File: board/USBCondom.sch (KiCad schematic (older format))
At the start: 8 parts, among them P1 To_Source, P2 To_Phone

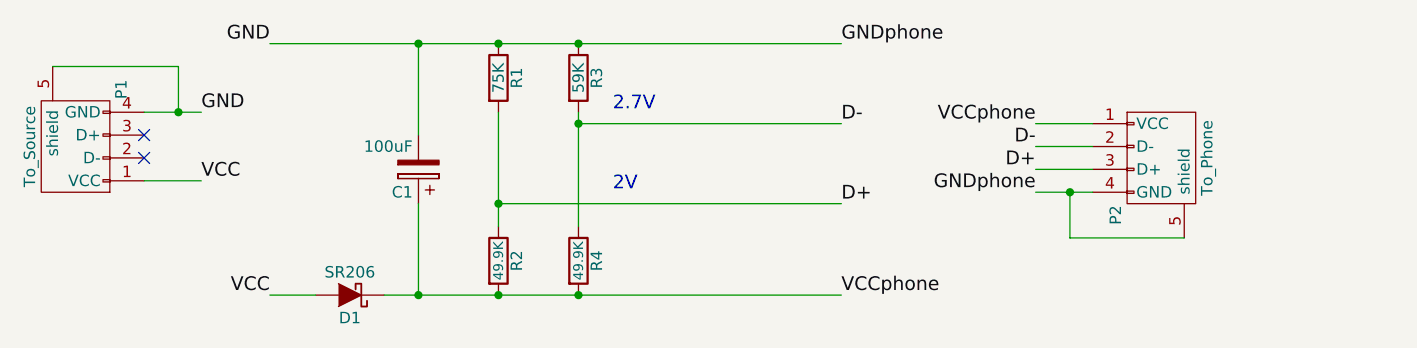
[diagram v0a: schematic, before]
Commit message: Update board to rev 2
Bugfixes:
* USB shields are no longer connected to GND

Updates:
* Changed C1 footprint to 1206_HandSoldering for larger pads
* Shrank down board size and made layout more compact
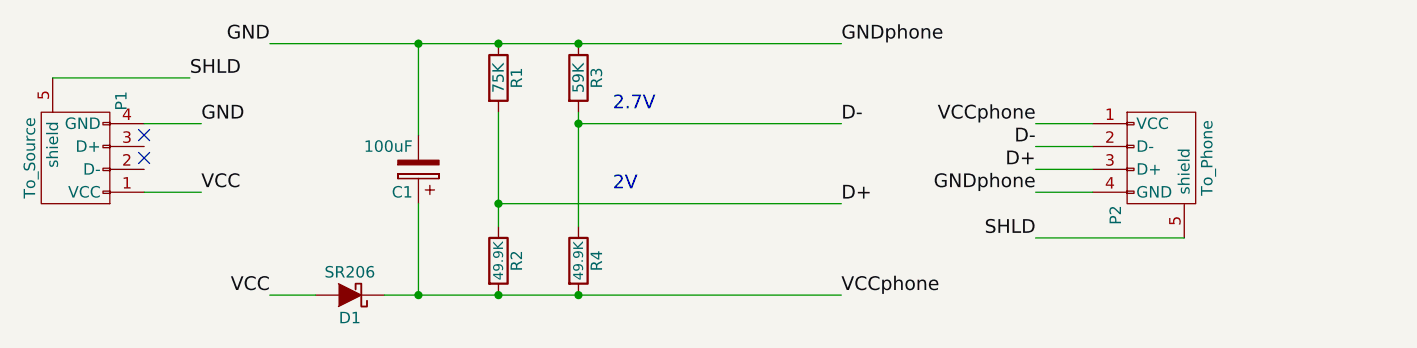
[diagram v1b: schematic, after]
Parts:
- C1: footprint Capacitors_SMD:C_1206 -> Capacitors_SMD:C_1206_HandSoldering
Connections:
- net GND: no longer P1.5 (shield), P2.5 (shield)
- new net SHLD: P1.5 (shield), P2.5 (shield)
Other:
- moved on the sheet: P1
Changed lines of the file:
@@
 Title "USB Condom"
 Date ""
-Rev "0.1"
+Rev "2"
 Comp "csammisrun"
 Comment1 ""
@@
 L USB_A P1
 U 1 1 58C0BE71
-P 1350 2800
-F 0 "P1" H 1550 2600 50  0000 C CNN
-F 1 "To_Source" H 1300 3000 50  0000 C CNN
-F 2 "Connect:USB_A" V 1300 2700 50  0001 C CNN
-F 3 "" V 1300 2700 50  0000 C CNN
-	1    1350 2800
+P 1350 2850
+F 0 "P1" H 1550 2650 50  0000 C CNN
+F 1 "To_Source" H 1300 3050 50  0000 C CNN
+F 2 "Connect:USB_A" V 1300 2750 50  0001 C CNN
+F 3 "" V 1300 2750 50  0000 C CNN
+	1    1350 2850
 	0    -1   -1   0
 $EndComp
@@
 F 0 "C1" H 2875 3050 50  0000 L CNN
 F 1 "100uF" H 2875 2850 50  0000 L CNN
-F 2 "Capacitors_SMD:C_1206" H 2888 2800 50  0001 C CNN
+F 2 "Capacitors_SMD:C_1206_HandSoldering" H 2888 2800 50  0001 C CNN
 F 3 "" H 2850 2950 50  0000 C CNN
 	1    2850 2950
@@
 	5800 2950 5550 2950
 Wire Wire Line
-	5550 3050 5800 3050
-Wire Wire Line
 	2850 3100 2850 3500
 Wire Wire Line
@@
 Connection ~ 2850 2400
 Connection ~ 2850 3500
-Wire Wire Line
-	5700 3050 5700 3250
-Wire Wire Line
-	5700 3250 6200 3250
-Connection ~ 5700 3050
 $Comp
 L R R3
@@
 Text Notes 3700 3050 0    60   ~ 0
 2V
-Wire Wire Line
-	1650 2700 1900 2700
-Wire Wire Line
-	1650 3000 1900 3000
 NoConn ~ 1650 2800
 NoConn ~ 1650 2900
-Text Label 1900 2700 0    60   ~ 0
+Text Label 1900 2750 0    60   ~ 0
 GND
-Text Label 1900 3000 0    60   ~ 0
+Text Label 1900 3050 0    60   ~ 0
 VCC
 Wire Wire Line
@@
 Text Label 2200 3500 2    60   ~ 0
 VCC
+Text Label 1850 2550 0    60   ~ 0
+SHLD
 Wire Wire Line
-	1800 2700 1800 2500
+	5800 3050 5550 3050
+Text Label 5550 3250 2    60   ~ 0
+SHLD
 Wire Wire Line
-	1800 2500 1250 2500
-Connection ~ 1800 2700
+	5550 3250 6200 3250
+Wire Wire Line
+	1250 2550 1850 2550
+Wire Wire Line
+	1650 2750 1900 2750
+Wire Wire Line
+	1900 3050 1650 3050
 $EndSCHEMATC

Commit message: Update board to rev 3
Bugfixes:
* USB device side no longer has Vcc and GND swapped

Updates:
* Rounded corners on PCB
* Extended PBC to give host side port more support
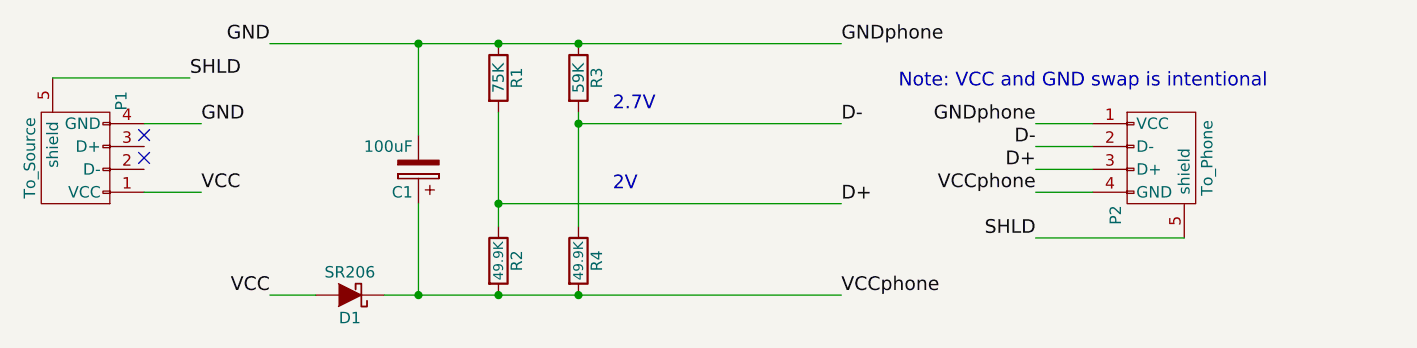
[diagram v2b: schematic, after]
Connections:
- net GND: now also P2.1 (VCC); no longer P2.4 (GND)
- net VCCphone: now also P2.4 (GND); no longer P2.1 (VCC)
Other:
- note added: "Note: VCC and GND swap is intentional"
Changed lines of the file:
@@
 Sheet 1 1
 Title "USB Condom"
-Date ""
-Rev "2"
+Date "2017-10-22"
+Rev "3"
 Comp "csammisrun"
 Comment1 ""
@@
 Text Label 4700 3500 0    60   ~ 0
 VCCphone
-Text Label 5550 2750 2    60   ~ 0
+Text Label 5550 3050 2    60   ~ 0
 VCCphone
 Text Label 5550 2850 2    60   ~ 0
@@
 Text Label 5550 2950 2    60   ~ 0
 D+
-Text Label 5550 3050 2    60   ~ 0
+Text Label 5550 2750 2    60   ~ 0
 GNDphone
 Wire Wire Line
@@
 Wire Wire Line
 	1900 3050 1650 3050
+Text Notes 4950 2600 0    60   ~ 0
+Note: VCC and GND swap is intentional
 $EndSCHEMATC
